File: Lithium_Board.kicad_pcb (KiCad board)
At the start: 6 copper layers, 80 x 67 mm, 120 parts, among them IC1 BQ25750RRVR, IC2 MCP1792T-3302H_DB, IC3 TCAN3414DDFR, IC4 STM32G0B1CET6N, IC6 BQ7694204PFBR, J1 XT30PW-M, J2 XT30PW-F, J3 XT30PW-M, J4 S3B-XH-SM4-TB_LF__SN_, J5 TSW-105-07-G-S, J6 Conn_01x06, J7 Conn_01x04, Q1 SIR870ADP-T1-GE3, Q10 MMBT5551LT1G, Q2 SIR870ADP-T1-GE3, Q3 SIR870ADP-T1-GE3, Q4 SIR870ADP-T1-GE3, Q5 SIR870ADP-T1-GE3, Q6 SIR870ADP-T1-GE3, Q7 SIR870ADP-T1-GE3, Q8 SIR870ADP-T1-GE3

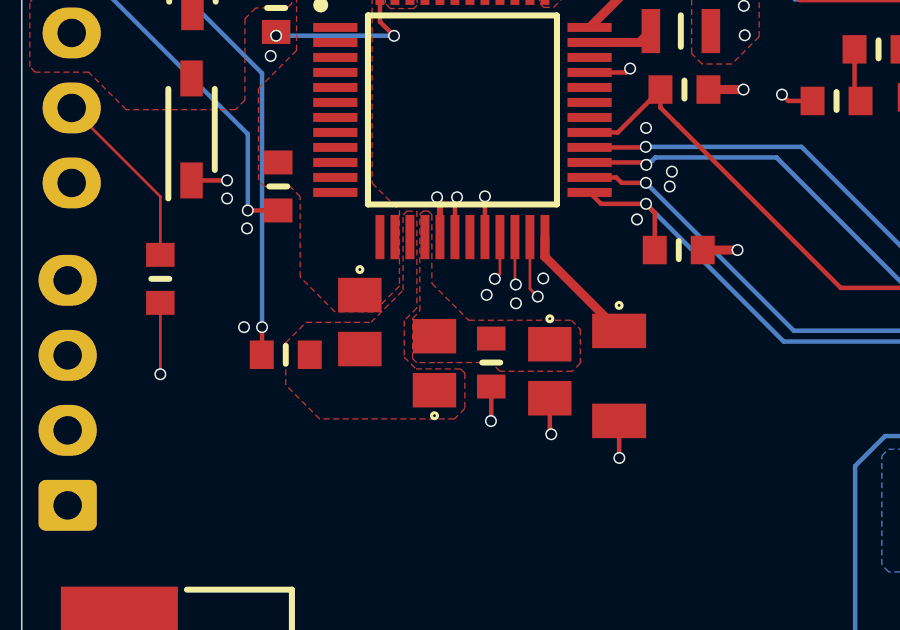
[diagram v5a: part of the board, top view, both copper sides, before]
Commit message: Cap to GND fixed
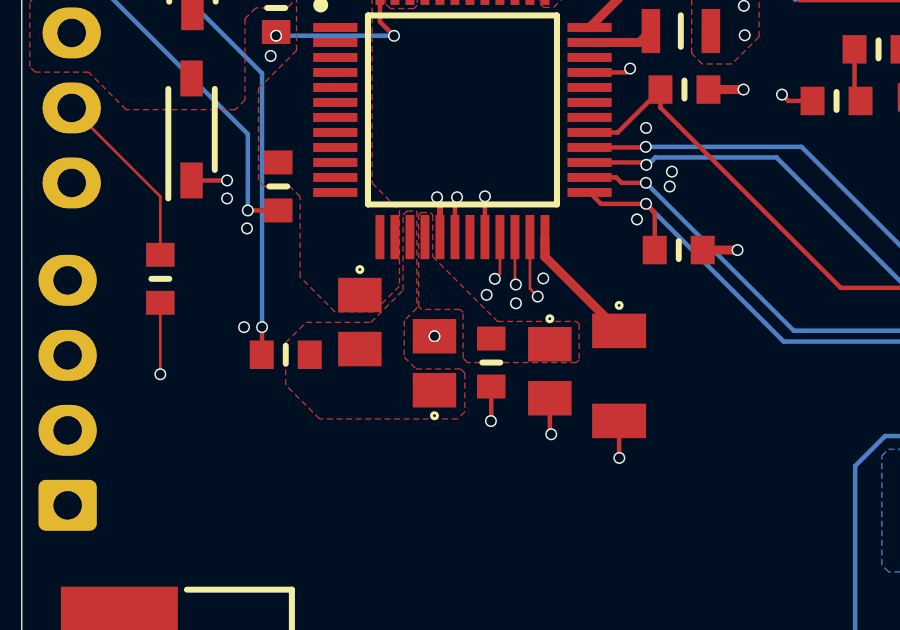
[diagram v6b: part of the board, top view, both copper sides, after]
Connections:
- C43 pad 2: /CELL BALANCING IC/VC0 -> GND
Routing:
- net GND: vias 175 -> 176
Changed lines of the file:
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@@
 			(size 1.15 1.45)
 			(layers "F.Cu" "F.Mask" "F.Paste")
-			(net 25 "/CELL BALANCING IC/VC0")
+			(net 1 "GND")
 			(pinfunction "2")
 			(pintype "passive")
@@
 	)
 	(via
+		(at 117.7175 100.9225)
+		(size 0.4)
+		(drill 0.3)
+		(layers "F.Cu" "B.Cu")
+		(net 1)
+	)
+	(via
 		(at 144.53 85.38)
 		(size 0.4)
@@
 	)
 	(zone
+		(net 25)
+		(net_name "/CELL BALANCING IC/VC0")
+		(layer "F.Cu")
+		(hatch edge 0.5)
+		(priority 28)
+		(connect_pads yes
+			(clearance 0.2)
+		)
+		(min_thickness 0.25)
+		(filled_areas_thickness no)
+		(fill yes
+			(thermal_gap 0.5)
+			(thermal_bridge_width 0.5)
+		)
+		(polygon
+			(pts
+				(xy 117.19 96.88) (xy 117.27 96.8) (xy 117.58 96.8) (xy 117.66 96.88) (xy 117.66 98.27) (xy 119.82 100.43)
+				(xy 122.46 100.43) (xy 122.54 100.51) (xy 122.54 101.71) (xy 122.45 101.8) (xy 118.82 101.8) (xy 118.67 101.65)
+				(xy 118.67 100.13) (xy 118.57 100.03) (xy 117.29 100.03) (xy 117.19 99.93)
+			)
+		)
+	)
+	(zone
 		(net 89)
 		(net_name "/Q7_DRAIN")
@@
 	)
 	(zone
-		(net 25)
-		(net_name "/CELL BALANCING IC/VC0")
-		(layer "F.Cu")
-		(hatch edge 0.5)
-		(priority 30)
-		(connect_pads yes
-			(clearance 0.2)
-		)
-		(min_thickness 0.25)
-		(filled_areas_thickness no)
-		(fill yes
-			(thermal_gap 0.5)
-			(thermal_bridge_width 0.5)
-		)
-		(polygon
-			(pts
-				(xy 117.23 96.86) (xy 117.34 96.75) (xy 117.51 96.75) (xy 117.63 96.87) (xy 117.63 99.16) (xy 118.86 100.39)
-				(xy 122.28 100.39) (xy 122.58 100.69) (xy 122.58 101.82) (xy 122.31 102.09) (xy 119.9 102.09) (xy 119.61 101.8)
-				(xy 117.74 101.8) (xy 117.7375 101.8025) (xy 117.1225 101.8025) (xy 116.99 101.67) (xy 116.99 100.33)
-				(xy 117.23 100.09)
-			)
-		)
-	)
-	(zone
 		(net 20)
 		(net_name "/CELL BALANCING IC/VC1")
@@
 				(xy 112.76 101.14) (xy 113.44 100.46) (xy 115.6 100.46) (xy 116.67 99.39) (xy 116.67 96.88) (xy 116.8 96.75)
 				(xy 117.13 96.75) (xy 117.13 99.98) (xy 116.71 100.4) (xy 116.71 101.62) (xy 117.1025 102.0125)
-				(xy 118.59 102.0125) (xy 118.73 102.1525) (xy 118.73 103.33) (xy 118.38 103.68) (xy 113.89 103.68)
+				(xy 118.59 102.0125) (xy 118.73 102.1525) (xy 118.73 103.44) (xy 118.49 103.68) (xy 113.89 103.68)
 				(xy 112.76 102.55)
 			)
